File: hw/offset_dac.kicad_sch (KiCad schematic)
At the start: 37 parts, among them Q1 SSM6N35AFE, Q3 SSM6N35AFE, U22 TSV992A, U23 MCP47CVB02-E_UN

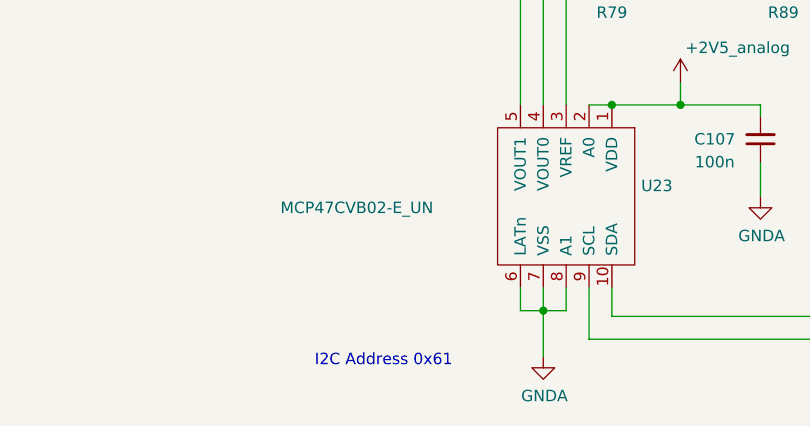
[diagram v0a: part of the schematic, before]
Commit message: fixed BOM; added relay drivers
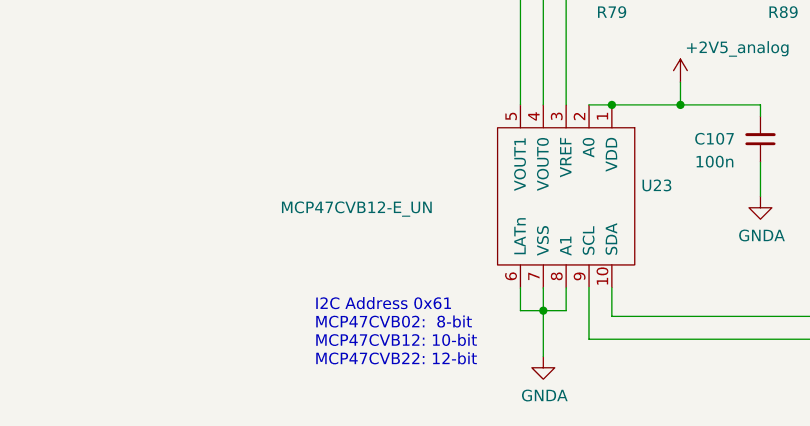
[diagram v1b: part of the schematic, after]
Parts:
- U23: value MCP47CVB02-E_UN -> MCP47CVB12-E_UN; Part MCP47CVB02-E/UN -> MCP47CVB12-E/UN
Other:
- note added: "I2C Address 0x61 MCP47CVB02: 8-bit MCP47CVB12: 10-bit MCP47CVB22: 12-bit"
- note removed: "I2C Address 0x61"
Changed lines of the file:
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@@
 		)
 	)
-	(text "I2C Address 0x61"
+	(text "I2C Address 0x61\nMCP47CVB02:  8-bit\nMCP47CVB12: 10-bit\nMCP47CVB22: 12-bit"
 		(exclude_from_sim no)
 		(at 77.47 171.45 0)
@@
 			)
 		)
-		(property "Value" "MCP47CVB02-E_UN"
+		(property "Value" "MCP47CVB12-E_UN"
 			(at 73.66 153.67 90)
 			(effects
@@
 			)
 		)
-		(property "Part" "MCP47CVB02-E/UN"
+		(property "Part" "MCP47CVB12-E/UN"
 			(at 105.41 152.4 0)
 			(effects

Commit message: connected versaclock CLKSEL to ULPI RSTB (share FPGA pin)
ULPI Rstb is unlikely to be used

Also: - update of kicad to 9.0 (many library footprints updated)
      - added sheet titles, author
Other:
- company: (none) -> Till Straumann
- title: (none) -> Calibration DAC

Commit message: Added licensing information
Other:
- company: Till Straumann -> Copyright Till Straumann, 2025
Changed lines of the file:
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@@
 		(title "Calibration DAC")
 		(rev "3.3b")
-		(company "Till Straumann")
-		(comment 1 "Range control with FET switches")
+		(company "Copyright Till Straumann, 2025")
+		(comment 1 "License: CERN-OHL-P v2")
 	)
 	(text "I2C Address 0x61\nMCP47CVB02:  8-bit\nMCP47CVB12: 10-bit\nMCP47CVB22: 12-bit"
